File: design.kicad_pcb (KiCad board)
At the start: 2 copper layers, 83.1 x 34.4 mm, 0 parts

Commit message: PCB add variables text block
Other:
- board text added: "<<project_name>> <<ID>> <<version>> <<date>> <<hash>> <<website_link>>"
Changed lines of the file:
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@@
   (net 0 "")
   (gr_rect (start 97.9 84.4) (end 181 118.8) (layer "Edge.Cuts") (width 0.05) (fill none))
+  (gr_text "<<project_name>>\n<<ID>>\n<<version>>\n<<date>>\n<<hash>>\n<<website_link>>" (at 139.6 101) (layer "B.SilkS")
+    (effects (font (size 1 1) (thickness 0.15)) (justify mirror))
+  )
 )

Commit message: Update design.kicad_pcb
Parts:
- added C1: 2.2pF, Capacitor_SMD:C_0805_2012Metric, F.Cu at (120.6, 98.6)
- added C2: 100pF, Capacitor_SMD:C_0805_2012Metric, F.Cu at (120.6, 95.6)
- added C3: 4.7uF, Capacitor_SMD:C_0805_2012Metric, F.Cu at (116.2, 98.6)
- added C4: 100pF, Capacitor_SMD:C_0805_2012Metric, F.Cu at (116.2, 95.6)
- added C5: 2.2uF, Capacitor_SMD:C_0805_2012Metric, F.Cu at (127.6, 91.1)
- added D1: BAT54C, Package_TO_SOT_SMD:SOT-23, F.Cu at (123.0, 91.9)
- added J1: Conn_01x06_Male, Connector_PinHeader_2.54mm:PinHeader_1x06_P2.54mm_Vertical, F.Cu at (111.6, 92.0)
- added JP1: Jumper_2_Open, TestPoint:TestPoint_Bridge_Pitch2.54mm_Drill1.0mm, F.Cu at (116.0, 91.7)
- added R1: 47ohm, Resistor_SMD:R_0805_2012Metric, F.Cu at (116.1, 101.6)
- added R2: 470ohm, Resistor_SMD:R_0805_2012Metric, F.Cu at (127.6, 94.1)
- added R3: 4.7k, Resistor_SMD:R_0805_2012Metric, F.Cu at (132.1, 91.1)
- added R4: 4.7k, Resistor_SMD:R_0805_2012Metric, F.Cu at (116.1, 104.5)
- added U1: IQS231A-00000000-TSR, Sensor_Touch_custom:SOT95P280X100-6N, F.Cu at (127.2, 103.0)

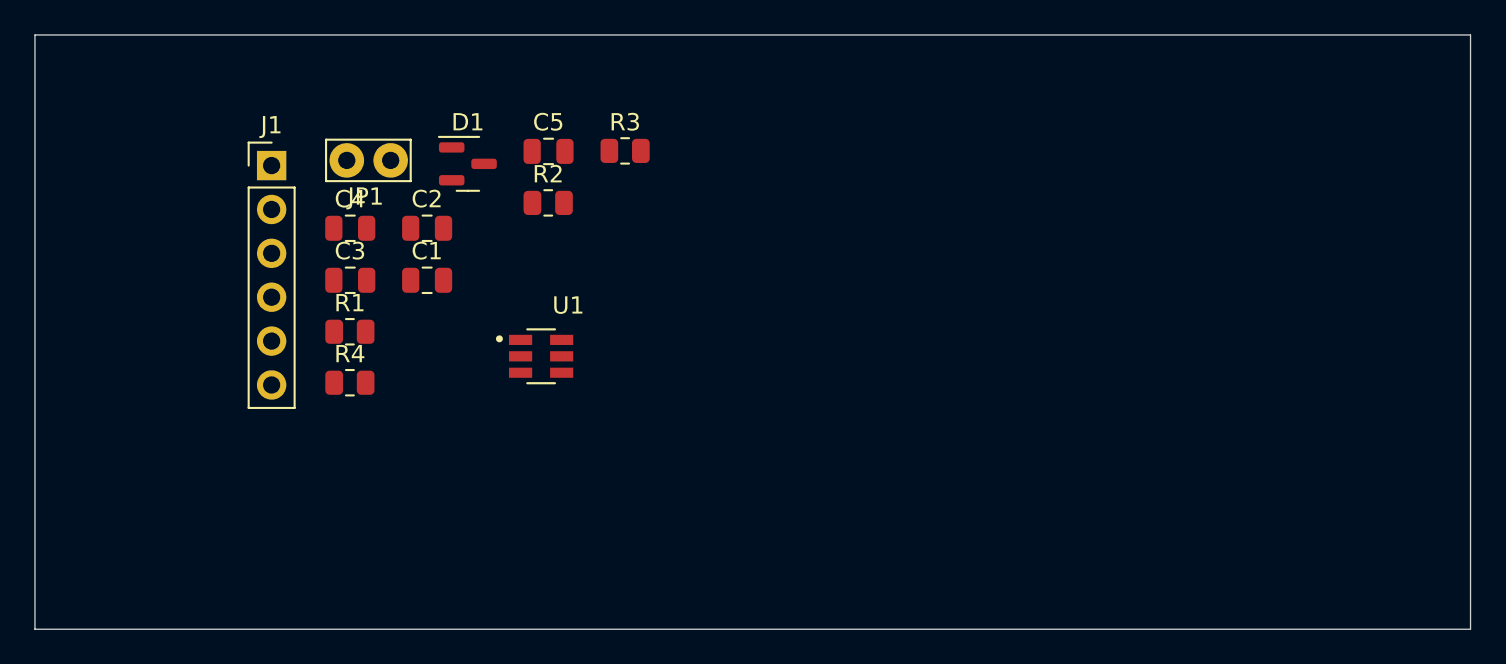
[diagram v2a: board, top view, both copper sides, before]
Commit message: pcb layout small sch changes for pcb
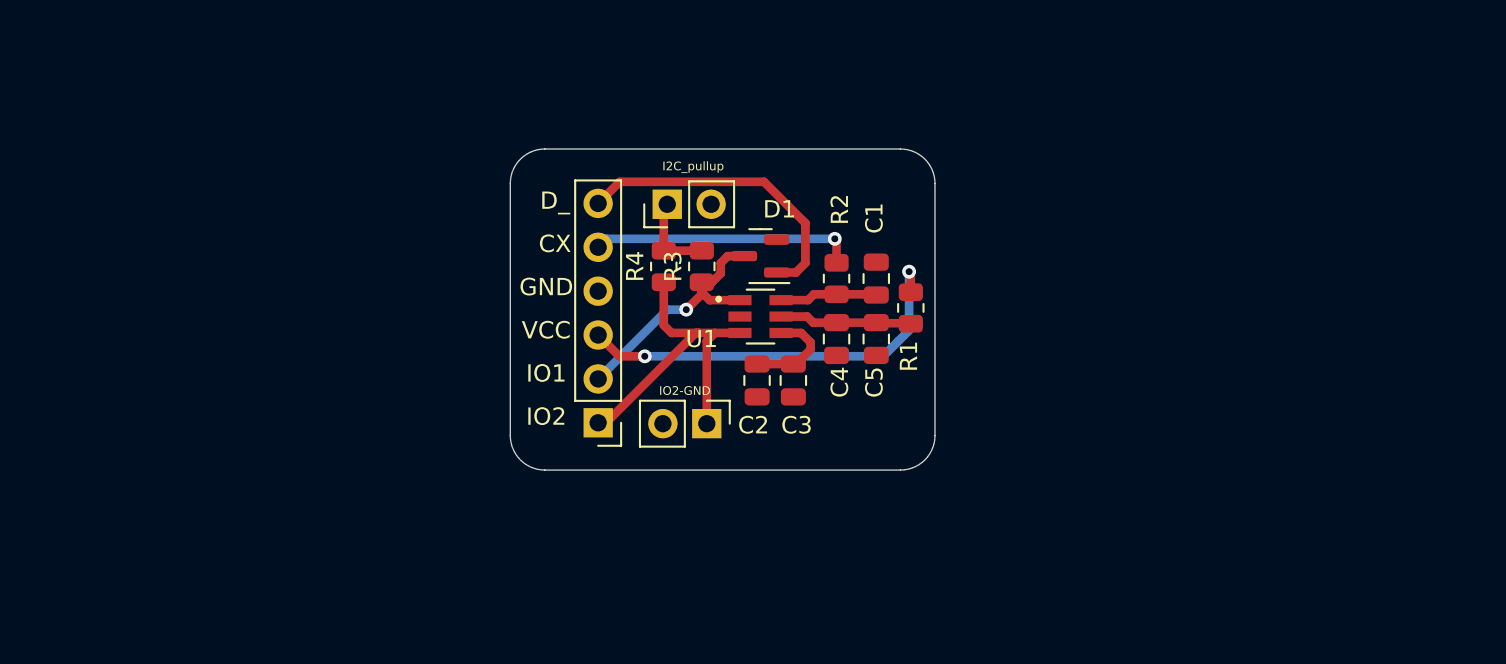
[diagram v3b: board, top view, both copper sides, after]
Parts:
- added JP2: I2C_pullup, Connector_PinHeader_2.54mm:PinHeader_1x02_P2.54mm_Vertical, F.Cu at (134.5, 94.2)
- JP1: value Jumper_2_Open -> IO2-GND; footprint TestPoint:TestPoint_Bridge_Pitch2.54mm_Drill1.0mm -> Connector_PinHeader_2.54mm:PinHeader_1x02_P2.54mm_Vertical
- moved R1 32.5 mm to (148.6, 100.2), turned to 90 degrees
- moved C4 28.9 mm to (144.3, 102.0), turned to -90 degrees
- moved C3 26.3 mm to (141.8, 104.4), turned to -90 degrees
- moved C1 26.0 mm to (146.6, 98.5), turned to 90 degrees
- moved JP1 25.8 mm to (136.8, 106.9), turned to -90 degrees
- moved J1 24.1 mm to (130.5, 106.8), turned to 180 degrees
- moved C5 21.9 mm to (146.6, 102.0), turned to -90 degrees
- moved C2 21.0 mm to (139.7, 104.4), turned to -90 degrees
- moved R4 19.4 mm to (134.3, 97.8), turned to 90 degrees
- moved D1 17.8 mm to (139.9, 97.2), turned to 180 degrees
- moved R2 17.3 mm to (144.3, 98.5), turned to -90 degrees
- moved U1 12.9 mm to (139.9, 100.7)
- moved R3 8.03 mm to (136.5, 97.8), turned to 90 degrees
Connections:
- net Net-(C1-Pad1) renamed /CX_ic
- net Net-(C2-Pad1) renamed /VREG
- net Net-(C4-Pad1) renamed /VCC_ic
- R3 pad 2: VCC -> Net-(R3-Pad2)
- R4 pad 2: VCC -> Net-(R3-Pad2)
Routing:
- net VCC: track 0.00 -> 23.8 mm, vias 0 -> 2
- net IO2/SDA: track 0.00 -> 20.5 mm
- net Net-(D1-Pad1): track 0.00 -> 17.7 mm
- net CX: track 0.00 -> 15.3 mm, vias 0 -> 1
- net IO1/SCL: track 0.00 -> 15.1 mm, vias 0 -> 1
- net /VCC_ic: track 0.00 -> 7.87 mm
- net /VREG: track 0.00 -> 5.79 mm
- net /CX_ic: track 0.00 -> 5.67 mm
- net Net-(R3-Pad2): track 0.00 -> 4.97 mm
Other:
- board size 83.1 x 34.4 mm -> 24.6 x 18.6 mm
- board text added: "CX"
- board text added: "D_"
- board text added: "GND"
- board text added: "IO1"
- board text added: "IO2"
- board text added: "VCC"

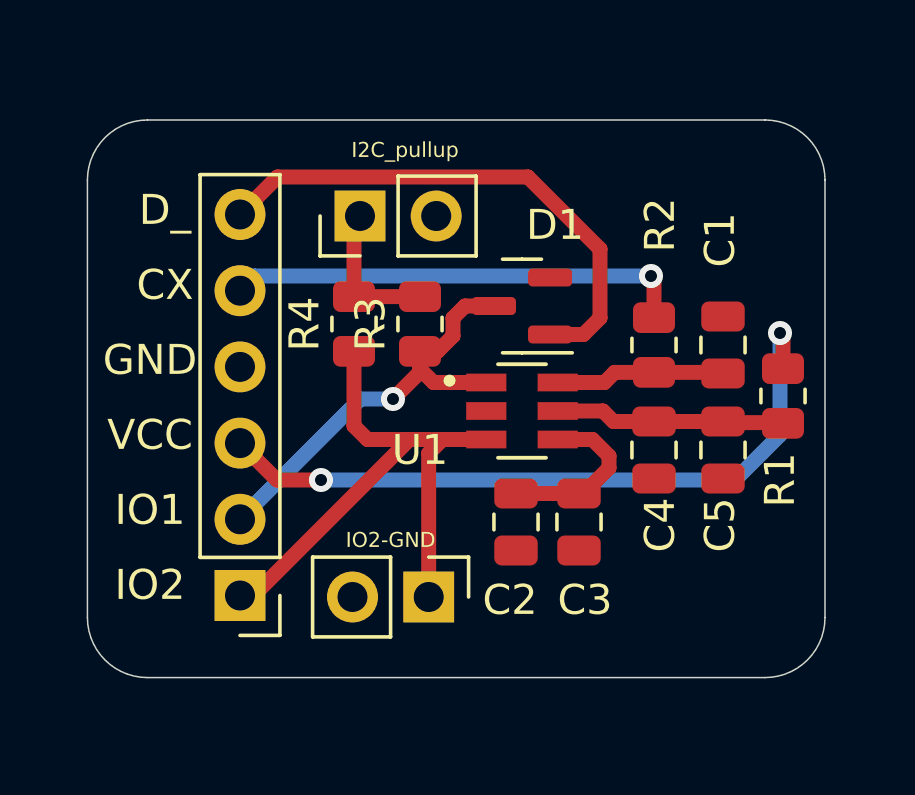
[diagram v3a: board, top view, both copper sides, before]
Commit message: add groundplane and DRC/ERC
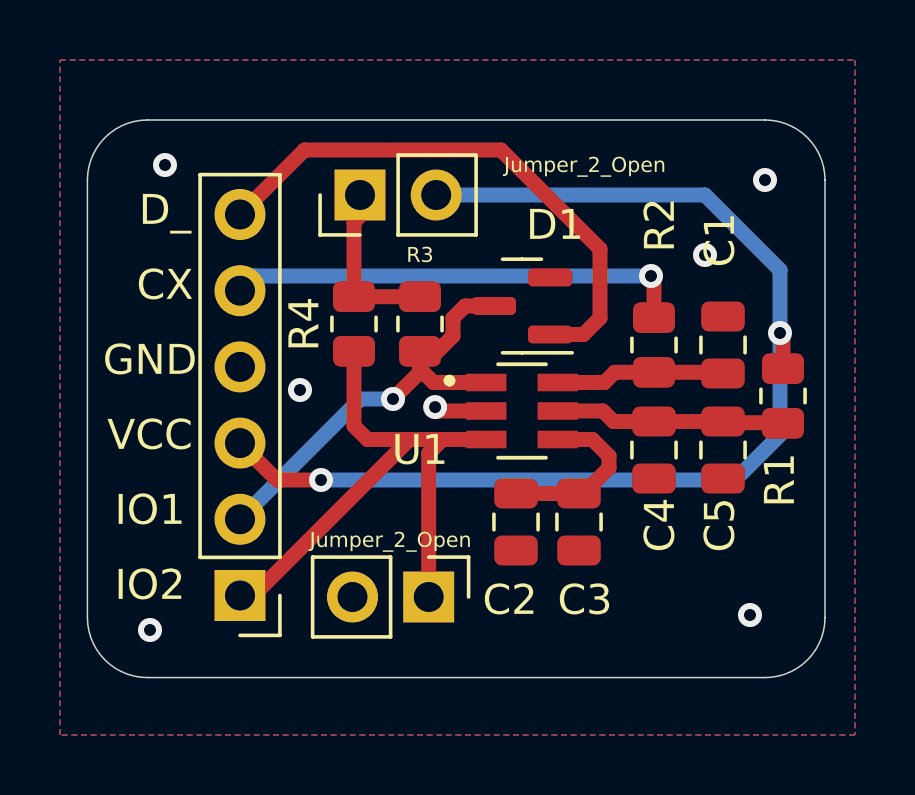
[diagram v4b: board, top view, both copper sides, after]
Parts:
- JP1: value IO2-GND -> Jumper_2_Open
- JP2: value I2C_pullup -> Jumper_2_Open
- moved JP2 0.70 mm to (134.5, 93.5)
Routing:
- net VCC: track 23.8 -> 38.4 mm
- net GND: track 0.00 -> 1.76 mm, vias 0 -> 7
- net Net-(D1-Pad1): track 17.7 -> 18.4 mm
- added copper zone on B.Cu, net GND
- added copper zone on F.Cu, net GND
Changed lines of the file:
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@@
     (property "Sheetname" "")
     (attr smd)
-    (fp_text reference "R3" (at 0 -1.65 90) (layer "F.SilkS")
-      (effects (font (size 1 1) (thickness 0.15)))
+    (fp_text reference "R3" (at 2.3 0 180) (layer "F.SilkS")
+      (effects (font (size 0.5 0.5) (thickness 0.1)))
     )
     (fp_text value "4.7k" (at 0 1.65 90) (layer "F.Fab")
@@
       (effects (font (size 1 1) (thickness 0.15)))
     )
-    (fp_text value "IO2-GND" (at -1.9 1.27) (layer "F.SilkS")
+    (fp_text value "Jumper_2_Open" (at -1.9 1.27) (layer "F.SilkS")
       (effects (font (size 0.5 0.5) (thickness 0.1)))
     )
@@
   )
   (footprint "Connector_PinHeader_2.54mm:PinHeader_1x02_P2.54mm_Vertical" (layer "F.Cu")
-    (at 134.5 94.2 90)
+    (at 134.5 93.5 90)
     (descr "Through hole straight pin header, 1x02, 2.54mm pitch, single row")
     (tags "Through hole pin header THT 1x02 2.54mm single row")
@@
       (effects (font (size 1 1) (thickness 0.15)))
     )
-    (fp_text value "I2C_pullup" (at 2.2 1.5 180) (layer "F.SilkS")
+    (fp_text value "Jumper_2_Open" (at 1 7.5 180) (layer "F.SilkS")
       (effects (font (size 0.5 0.5) (thickness 0.1)))
     )
@@
   (segment (start 139.7 103.45) (end 141.8 103.45) (width 0.5) (layer "F.Cu") (net 1))
   (segment (start 142.8 102.6) (end 142.8 102.2) (width 0.5) (layer "F.Cu") (net 1))
+  (segment (start 138.71 100.7) (end 137.135012 100.7) (width 0.5) (layer "F.Cu") (net 2))
+  (segment (start 137.135012 100.7) (end 137.004512 100.5695) (width 0.5) (layer "F.Cu") (net 2))
+  (via (at 128 92.5) (size 0.8) (drill 0.4) (layers "F.Cu" "B.Cu") (free) (net 2))
+  (via (at 147.5 107.5) (size 0.8) (drill 0.4) (layers "F.Cu" "B.Cu") (free) (net 2))
+  (via (at 127.5 108) (size 0.8) (drill 0.4) (layers "F.Cu" "B.Cu") (free) (net 2))
+  (via (at 137.004512 100.5695) (size 0.8) (drill 0.4) (layers "F.Cu" "B.Cu") (net 2))
+  (via (at 146 95.5) (size 0.8) (drill 0.4) (layers "F.Cu" "B.Cu") (free) (net 2))
+  (via (at 132.5 100) (size 0.8) (drill 0.4) (layers "F.Cu" "B.Cu") (free) (net 2))
+  (via (at 148 93) (size 0.8) (drill 0.4) (layers "F.Cu" "B.Cu") (free) (net 2))
   (segment (start 141.09 99.75) (end 142.65 99.75) (width 0.5) (layer "F.Cu") (net 3))
   (segment (start 142.9875 99.4125) (end 144.3 99.4125) (width 0.5) (layer "F.Cu") (net 3))
@@
   (segment (start 134.3 96.8875) (end 134.3 94.4) (width 0.5) (layer "F.Cu") (net 4))
   (segment (start 136.5 96.8875) (end 134.3 96.8875) (width 0.5) (layer "F.Cu") (net 4))
-  (segment (start 131.75 92.9) (end 130.5 94.15) (width 0.5) (layer "F.Cu") (net 5))
-  (segment (start 142.5 95.3) (end 140.1 92.9) (width 0.5) (layer "F.Cu") (net 5))
-  (segment (start 140.1 92.9) (end 131.75 92.9) (width 0.5) (layer "F.Cu") (net 5))
+  (segment (start 139.2 92) (end 132.65 92) (width 0.5) (layer "F.Cu") (net 5))
+  (segment (start 141.95 98.15) (end 142.5 97.6) (width 0.5) (layer "F.Cu") (net 5))
+  (segment (start 142.5 95.3) (end 139.2 92) (width 0.5) (layer "F.Cu") (net 5))
+  (segment (start 132.65 92) (end 130.5 94.15) (width 0.5) (layer "F.Cu") (net 5))
+  (segment (start 140.8375 98.15) (end 141.95 98.15) (width 0.5) (layer "F.Cu") (net 5))
   (segment (start 142.5 97.6) (end 142.5 95.3) (width 0.5) (layer "F.Cu") (net 5))
-  (segment (start 141.95 98.15) (end 142.5 97.6) (width 0.5) (layer "F.Cu") (net 5))
-  (segment (start 140.8375 98.15) (end 141.95 98.15) (width 0.5) (layer "F.Cu") (net 5))
   (segment (start 137.6 97.6) (end 137.6 98.2) (width 0.5) (layer "F.Cu") (net 7))
   (segment (start 136.95 99.75) (end 138.71 99.75) (width 0.5) (layer "F.Cu") (net 7))
@@
   (segment (start 147.9 102.1) (end 147 103) (width 0.5) (layer "B.Cu") (net 9))
   (segment (start 148.5 101.5) (end 147.9 102.1) (width 0.5) (layer "B.Cu") (net 9))
+  (segment (start 146 93.5) (end 137.04 93.5) (width 0.5) (layer "B.Cu") (net 9))
   (segment (start 148.5 98.1) (end 148.5 101.5) (width 0.5) (layer "B.Cu") (net 9))
   (segment (start 147 103) (end 133.2 103) (width 0.5) (layer "B.Cu") (net 9))
+  (segment (start 148.5 98.1) (end 148.5 96) (width 0.5) (layer "B.Cu") (net 9))
+  (segment (start 148.5 96) (end 146 93.5) (width 0.5) (layer "B.Cu") (net 9))
   (segment (start 144.3 97.5875) (end 144.3 96.3) (width 0.5) (layer "F.Cu") (net 10))
   (segment (start 144.3 96.3) (end 144.2 96.2) (width 0.5) (layer "F.Cu") (net 10))
@@
   (segment (start 146.5625 101.05) (end 146.6 101.0875) (width 0.5) (layer "F.Cu") (net 11))
   (segment (start 141.09 100.7) (end 142.6 100.7) (width 0.5) (layer "F.Cu") (net 11))
-  (segment (start 148.6375 101.0875) (end 148.75 101.2) (width 0.5) (layer "F.Cu") (net 11))
   (segment (start 144.3 101.05) (end 146.5625 101.05) (width 0.5) (layer "F.Cu") (net 11))
   (segment (start 142.95 101.05) (end 144.3 101.05) (width 0.5) (layer "F.Cu") (net 11))
+  (zone (net 2) (net_name "GND") (layers F&B.Cu) (hatch edge 0.508)
+    (connect_pads (clearance 0.508))
+    (min_thickness 0.254) (filled_areas_thickness no)
+    (fill yes (thermal_gap 0.508) (thermal_bridge_width 0.508))
+    (polygon
+      (pts
+        (xy 151 111.5)
+        (xy 124.5 111.5)
+        (xy 124.5 89)
+        (xy 151 89)
+      )
+    )
+  )
 )
